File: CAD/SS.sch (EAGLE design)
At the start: 88 parts, among them Q1 SN74AHC-NOR, Q2 UMD5N, Q4 SN74AHC-AND, Q5 BFP460, Q6 L78L05, Q7 NCP553, T1 MMBTRA104SS

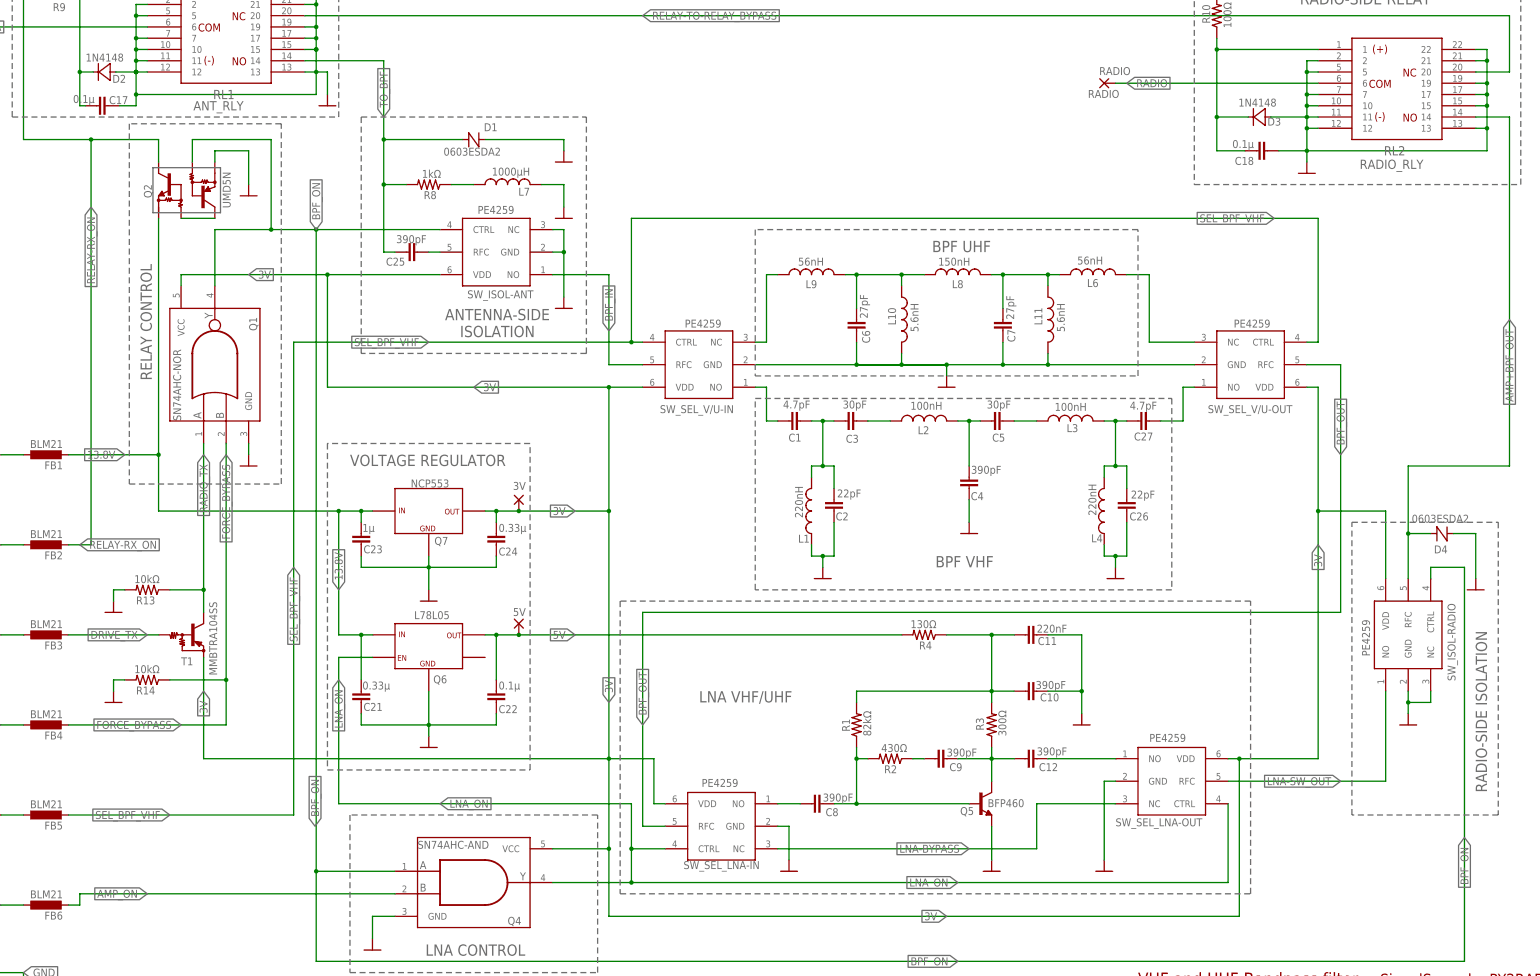
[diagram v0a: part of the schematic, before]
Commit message: More improvements, check the commit comment
- Fixed BFR460 footprint (it was VERY wrong)
- Zeroed the DRC warnings
- Added rastnest stop on some large RF-involved components
- Named few signal lines
- Improved identification of Pin 1 of RF switches
- Added Test Points
- Better component identification
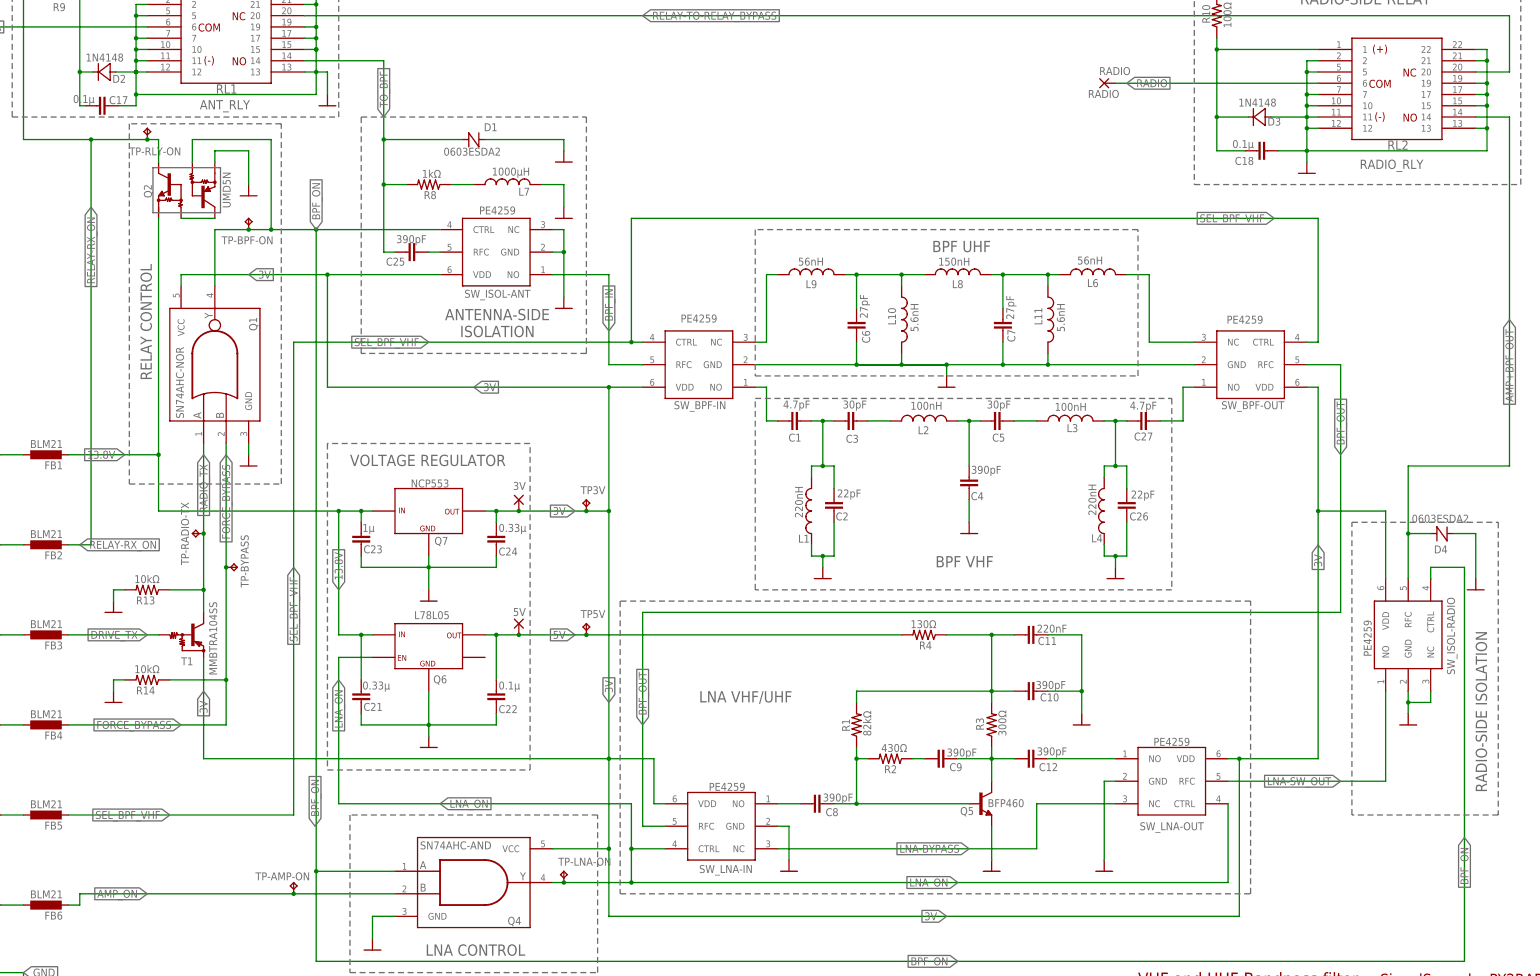
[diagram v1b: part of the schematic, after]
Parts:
- added TP-AMP-ON, TP-BPF-ON, TP-BYPASS, TP-LNA-ON, TP-RADIO-TX, TP-RLY-ON, TP3V, TP5V: TPB1,27, testpad:TPB1,27
- Q5: device aarf:BFR193F -> aarf:BFP460
- renumbered SW_SEL_LNA-IN to SW_LNA-IN, SW_SEL_LNA-OUT to SW_LNA-OUT, SW_SEL_V/U-IN to SW_BPF-IN, SW_SEL_V/U-OUT to SW_BPF-OUT
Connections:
- net N$17 renamed LNA-IN
- net N$25 renamed LNA-OUT
- net 3V: now also TP3V.TP
- net 5V: now also TP5V.TP
- net AMP_ON: now also TP-AMP-ON.TP
- net BPF_ON: now also TP-BPF-ON.TP
- net FORCE_BYPASS: now also TP-BYPASS.TP
- net LNA_ON: now also TP-LNA-ON.TP
- net RADIO_TX: now also TP-RADIO-TX.TP
- net RELAY-RX_ON: now also TP-RLY-ON.TP

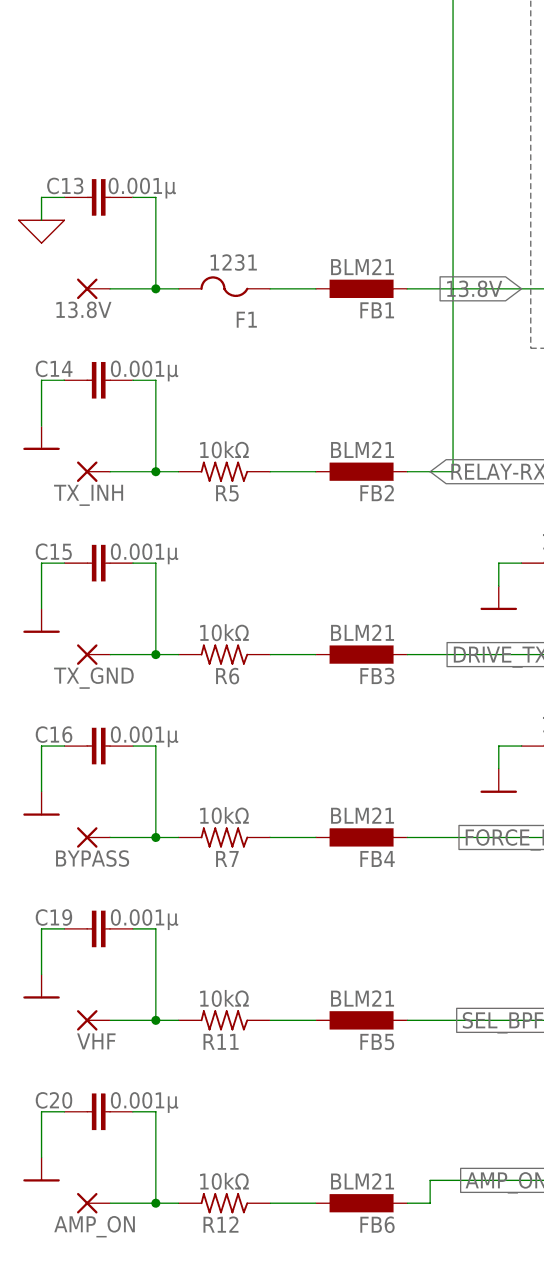
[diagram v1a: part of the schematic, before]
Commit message: New: BOM. And minor improvements (more in comments)
- Added a BOM
- Changed L7 footprint to match the Tayo proprietary (1207 footprint)
- Another round of DRC check
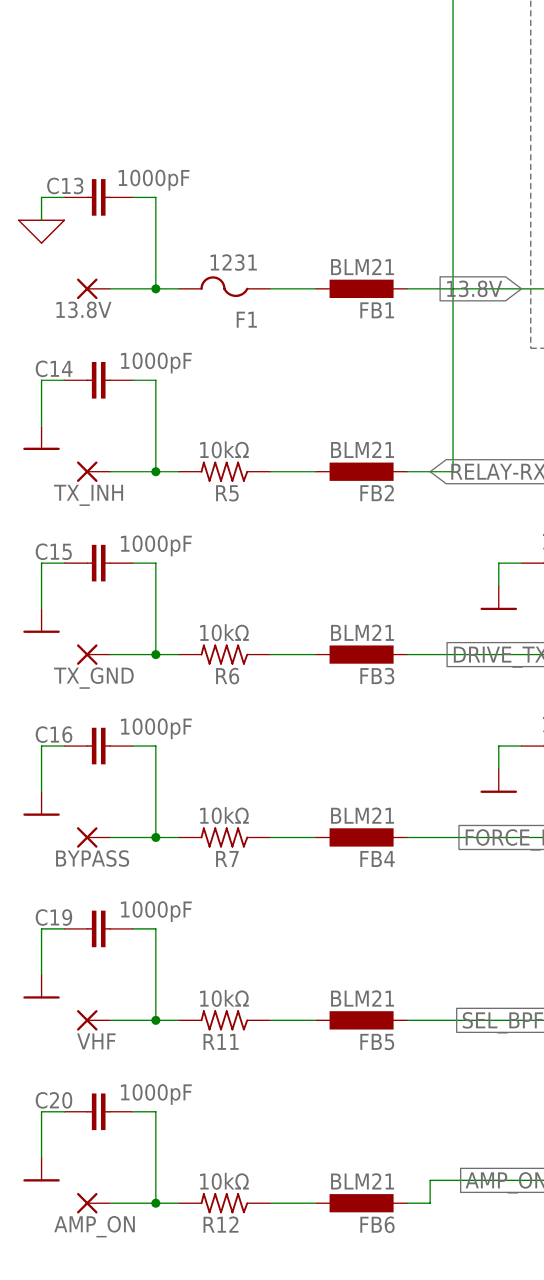
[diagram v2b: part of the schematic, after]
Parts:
- C13, C14, C15, C16, C19, C20: value 0.001µ -> 1000pF
- L7: device aarf:L-0805 -> aarf:L-1207
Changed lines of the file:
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@@
 <part name="FB2" library="aarf" deviceset="FB-0805" device="" value="BLM21"/>
 <part name="R5" library="aarf" deviceset="R-1206" device="" value="10kΩ"/>
-<part name="C13" library="aarf" deviceset="C-0805" device="" value="0.001µ"/>
-<part name="C14" library="aarf" deviceset="C-0805" device="" value="0.001µ"/>
+<part name="C13" library="aarf" deviceset="C-0805" device="" value="1000pF"/>
+<part name="C14" library="aarf" deviceset="C-0805" device="" value="1000pF"/>
 <part name="X_8" library="ngspice-simulation" library_urn="urn:adsk.eagle:library:527439" deviceset="GND" device=""/>
 <part name="R6" library="aarf" deviceset="R-1206" device="" value="10kΩ"/>
 <part name="FB3" library="aarf" deviceset="FB-0805" device="" value="BLM21"/>
-<part name="C15" library="aarf" deviceset="C-0805" device="" value="0.001µ"/>
+<part name="C15" library="aarf" deviceset="C-0805" device="" value="1000pF"/>
 <part name="Q1" library="aarf" deviceset="SN74AHC-NOR" device="" package3d_urn="urn:adsk.eagle:package:2405/1"/>
-<part name="C16" library="aarf" deviceset="C-0805" device="" value="0.001µ"/>
+<part name="C16" library="aarf" deviceset="C-0805" device="" value="1000pF"/>
 <part name="BYPASS" library="wirepad" library_urn="urn:adsk.eagle:library:412" deviceset="SMD2" device="" package3d_urn="urn:adsk.eagle:package:30839/1" value="BYPASS"/>
 <part name="R7" library="aarf" deviceset="R-1206" device="" value="10kΩ"/>
@@
 <part name="C18" library="aarf" deviceset="C-0805" device="" value="0.1µ"/>
 <part name="R10" library="aarf" deviceset="R-1206" device="" value="100Ω"/>
-<part name="C19" library="aarf" deviceset="C-0805" device="" value="0.001µ"/>
+<part name="C19" library="aarf" deviceset="C-0805" device="" value="1000pF"/>
 <part name="VHF" library="wirepad" library_urn="urn:adsk.eagle:library:412" deviceset="SMD2" device="" package3d_urn="urn:adsk.eagle:package:30839/1" value="VHF"/>
 <part name="R11" library="aarf" deviceset="R-1206" device="" value="10kΩ"/>
 <part name="FB5" library="aarf" deviceset="FB-0805" device="" value="BLM21"/>
-<part name="C20" library="aarf" deviceset="C-0805" device="" value="0.001µ"/>
+<part name="C20" library="aarf" deviceset="C-0805" device="" value="1000pF"/>
 <part name="AMP_ON" library="wirepad" library_urn="urn:adsk.eagle:library:412" deviceset="SMD2" device="" package3d_urn="urn:adsk.eagle:package:30839/1" value="AMP_ON"/>
 <part name="R12" library="aarf" deviceset="R-1206" device="" value="10kΩ"/>
@@
 <part name="T1" library="transistor" library_urn="urn:adsk.eagle:library:402" deviceset="*-PNP_DRIVER-" device="SC59-BEC" package3d_urn="urn:adsk.eagle:package:28754/2" technology="MUN2111T1" value="MMBTRA104SS"/>
 <part name="R8" library="aarf" deviceset="R-1206" device="" value="1kΩ"/>
-<part name="L7" library="aarf" deviceset="L-0805" device="" value="1000µH"/>
+<part name="L7" library="aarf" deviceset="L-1207" device="" value="1000µH"/>
 <part name="R13" library="aarf" deviceset="R-1206" device="" value="10kΩ"/>
 <part name="R14" library="aarf" deviceset="R-1206" device="" value="10kΩ"/>
@@
 <instance part="C13" gate="G$1" x="12.7" y="162.56" smashed="yes" rot="R90">
 <attribute name="NAME" x="12.446" y="164.719" size="1.778" layer="95" rot="R180"/>
-<attribute name="VALUE" x="22.606" y="164.719" size="1.778" layer="96" rot="R180"/>
+<attribute name="VALUE" x="20.066" y="164.719" size="1.778" layer="96" rot="R180" align="center"/>
 </instance>
 <instance part="C14" gate="G$1" x="12.7" y="142.24" smashed="yes" rot="R90">
 <attribute name="NAME" x="11.176" y="144.399" size="1.778" layer="95" rot="R180"/>
-<attribute name="VALUE" x="22.86" y="144.399" size="1.778" layer="96" rot="R180"/>
+<attribute name="VALUE" x="20.32" y="144.399" size="1.778" layer="96" rot="R180" align="center"/>
 </instance>
 <instance part="X_8" gate="G$1" x="7.62" y="160.02" smashed="yes"/>
@@
 <instance part="C15" gate="G$1" x="12.7" y="121.92" smashed="yes" rot="R90">
 <attribute name="NAME" x="11.176" y="124.079" size="1.778" layer="95" rot="R180"/>
-<attribute name="VALUE" x="22.86" y="124.079" size="1.778" layer="96" rot="R180"/>
+<attribute name="VALUE" x="20.32" y="124.079" size="1.778" layer="96" rot="R180" align="center"/>
 </instance>
 <instance part="Q1" gate="G$1" x="81.28" y="172.72" smashed="yes" rot="R90">
@@
 <instance part="C16" gate="G$1" x="12.7" y="101.6" smashed="yes" rot="R90">
 <attribute name="NAME" x="11.176" y="103.759" size="1.778" layer="95" rot="R180"/>
-<attribute name="VALUE" x="22.86" y="103.759" size="1.778" layer="96" rot="R180"/>
+<attribute name="VALUE" x="20.32" y="103.759" size="1.778" layer="96" rot="R180" align="center"/>
 </instance>
 <instance part="BYPASS" gate="1" x="12.7" y="91.44" smashed="yes">
@@
 <instance part="C19" gate="G$1" x="12.7" y="81.28" smashed="yes" rot="R90">
 <attribute name="NAME" x="11.176" y="83.439" size="1.778" layer="95" rot="R180"/>
-<attribute name="VALUE" x="22.86" y="83.439" size="1.778" layer="96" rot="R180"/>
+<attribute name="VALUE" x="20.32" y="83.439" size="1.778" layer="96" rot="R180" align="center"/>
 </instance>
 <instance part="VHF" gate="1" x="12.7" y="71.12" smashed="yes">
@@
 <instance part="C20" gate="G$1" x="12.7" y="60.96" smashed="yes" rot="R90">
 <attribute name="NAME" x="11.176" y="63.119" size="1.778" layer="95" rot="R180"/>
-<attribute name="VALUE" x="22.86" y="63.119" size="1.778" layer="96" rot="R180"/>
+<attribute name="VALUE" x="20.32" y="63.119" size="1.778" layer="96" rot="R180" align="center"/>
 </instance>
 <instance part="AMP_ON" gate="1" x="12.7" y="50.8" smashed="yes">

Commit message: Starring: Rev. B
Resolves: #1 #2 #4 #5 #10 #11 #12 #13 #14 #15 #16 #17

In a nutshell:
- Fixed UMD5N placement issue
- Improved UMD5N footprint
- Improved NCP553 footprint
- Improved SN74-OR footprint
- Changed connectors to SMA
- Fixed the 5V voltage regulator
- Fixed lotsa BOM errors
- Improved and recalculated coplanar waveguide
- Updated VHF BPF component values
- Added a TP for VHF BPF
- Added three u.FL connectors/pads to help debugging
- Pretty much this is it!
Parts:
- removed ANTENNA: ANTENNA, wirepad:SMD2
- removed RADIO: RADIO, wirepad:SMD2
- added TP-VHF-ON: TPB1,27, testpad:TPB1,27
- added X1: ANTENNA, aarf:SMA-PCB
- added X2: RADIO, aarf:SMA-PCB
- added X3: INP, adafruit:ANTENNA_U.FL
- added X4: AMP-O, adafruit:ANTENNA_U.FL
- added X5: BPF-O, adafruit:ANTENNA_U.FL
- C1, C27: value 4.7pF -> 6.8pF
- C10, C12, C8, C9: device aarf:MURATACAP -> aarf:C-0805
- C11: value 220nF -> 0.22µF; device aarf:MURATACAP -> aarf:C-0805
- C2, C26: value 22pF -> 24pF
- C21: value 0.33µ -> 0.47µ
- C22: value 0.1µ -> 0.47µ
- C3, C5: value 30pF -> 22pF
- L1, L4: value 220nH -> 150nH
- Q6: value L78L05 -> TCR1HF50; device aarf:MIC5365 -> aarf:TCR1HF
- renumbered SW_ISOL-ANT to SW-IS-ANT, SW_ISOL-RADIO to SW-IS-RAD
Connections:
- removed net IN_DECPL: C25.2, SW-IS-ANT.RFC
- removed net N$36: Q2.2, Q2.3
- new net N$17: C25.1, SW-IS-ANT.RFC, X3.SIGNAL
- new net N$7: Q2.4, Q2.5
- net 13.8V: now also Q2.6; no longer Q2.1
- net AMP+BPF_OUT: now also X4.SIGNAL
- net ANTENNA: now also X1.1; no longer ANTENNA.P
- net BPF_ON: now also Q2.2; no longer Q2.5
- net BPF_OUT: now also X5.SIGNAL
- net GND: now also Q2.1, X1.2, X2.2, X3.GND@1, X4.GND@1, X5.GND@1; no longer Q2.6
- net RADIO: now also X2.1; no longer RADIO.P
- net RELAY-RX_ON: now also Q2.3; no longer Q2.4
- net SEL_BPF_VHF: now also TP-VHF-ON.TP
- net TO_BPF: now also C25.2; no longer C25.1
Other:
- note added: "VOLTAGE REGULATORS"
- note removed: "VOLTAGE REGULATOR"
- moved on the sheet: C25, Q2

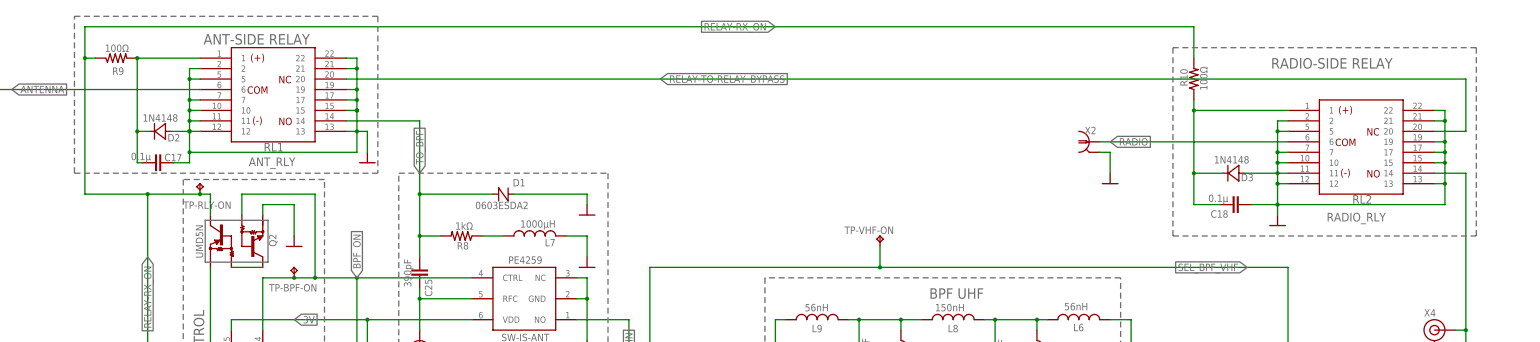
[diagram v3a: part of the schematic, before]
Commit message: Revision B updates
- Added a detachable board (taking advantage of the spare board real estate) that fits a RTL-SDR Bandpass filter.
- Minor signal and label revisions, routing
- Better labeling for signal I/O by adding expected voltages, improved semiotics
- Tentatively final.
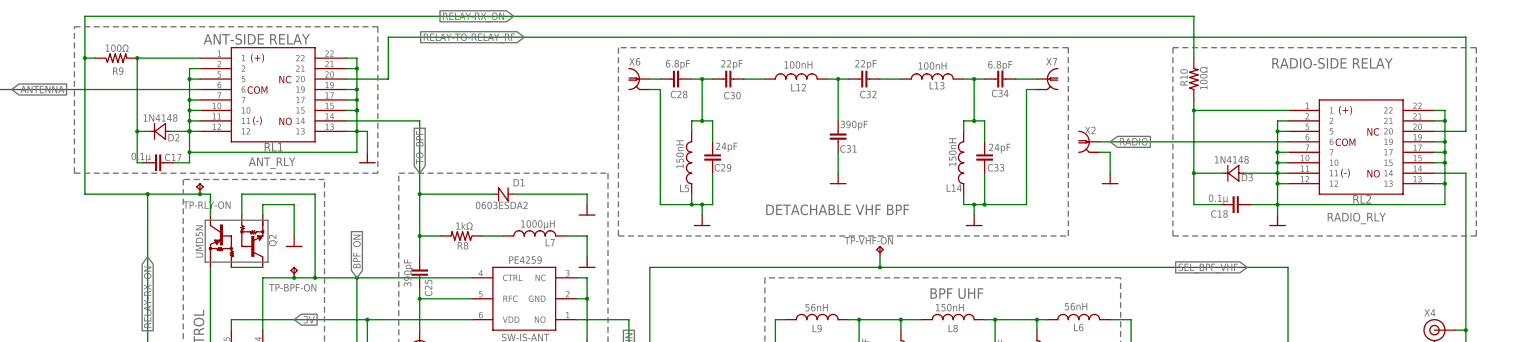
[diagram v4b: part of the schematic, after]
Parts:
- added C28, C34: 6.8pF, aarf:MURATACAP
- added C29, C33: 24pF, aarf:MURATACAP
- added C30, C32: 22pF, aarf:MURATACAP
- added C31: 390pF, aarf:MURATACAP
- added L12, L13: 100nH, aarf:L-0805
- added L14, L5: 150nH, aarf:L-0805
- added X6, X7: (no value), aarf:SMA-EDGE
- C10, C12, C8, C9: device aarf:C-0805 -> aarf:MURATACAP
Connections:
- net RELAY-TO-RELAY_BYPASS renamed RELAY-TO-RELAY_RF
- new net N$18: C28.1, C29.1, C30.2, L5.2
- new net N$20: C30.1, L12.1
- new net N$21: C31.1, C32.1, L12.2
- new net N$23: C33.1, C34.1, L13.2, L14.1
- new net N$25: C32.2, L13.1
- new net VHF-IN1: C28.2, X6.1
- new net VHF-OUT1: C34.2, X7.1
- net GND: now also C29.2, C31.2, C33.2, L14.2, L5.1, X6.2, X7.2
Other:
- note added: "DETACHABLE VHF BPF"
- moved on the sheet: TP-VHF-ON
